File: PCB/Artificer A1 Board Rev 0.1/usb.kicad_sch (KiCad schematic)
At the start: 24 parts, among them U11 CH217K, U3 CH334F_C5187527, U5 CH217K, U6 GT-USB-7010ASV, X1 SMD-3225_4P12M12PF10PPM

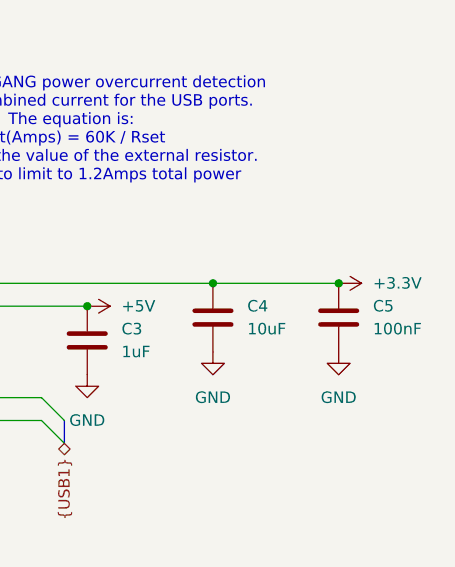
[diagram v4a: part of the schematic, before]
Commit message: added: sd, wifi, audio, started power, fixed buses
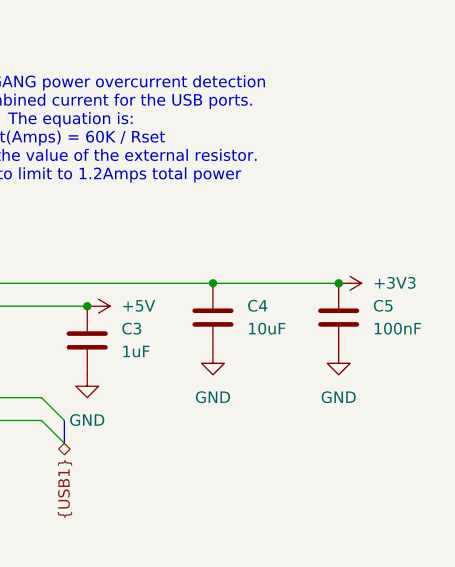
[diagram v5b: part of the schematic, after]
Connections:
- net +3.3V renamed +3V3
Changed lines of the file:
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@@
 		(company "Matthew Spotten")
 	)
-	(bus_alias "HS"
-		(members "RGMII0-PHYRSTB" "RGMII0-MDC" "RGMII0-MDIO" "RGMII0-TXD3" "RGMII0-TXD2"
-			"GMII0-TXD1" "RGMII0-TXD0" "RGMII0-TXCTL" "RGMII0-TXCK" "RGMII0-INTB"
-			"RGMII0-RXCK" "RGMII0-RXCTL" "RGMII0-RXD0" "RGMII0-RXD1" "RGMII0-RXD2"
-			"RGMII0-RXD3"
-		)
-	)
 	(text "PSELF is pulled high internally to\ntell the hub controller that it is\nself powered.\n"
 		(exclude_from_sim no)
@@
 	)
 	(junction
+		(at 267.97 66.04)
+		(diameter 0)
+		(color 0 0 0 0)
+	)
+	(junction
 		(at 121.92 73.66)
 		(diameter 0)
@@
 	)
 	(junction
-		(at 267.97 66.04)
-		(diameter 0)
-		(color 0 0 0 0)
-	)
-	(junction
 		(at 33.02 58.42)
 		(diameter 0)
@@
 	)
 	(symbol
-		(lib_id "power:+3.3V")
-		(at 267.97 66.04 270)
-		(unit 1)
-		(exclude_from_sim no)
-		(in_bom yes)
-		(on_board yes)
-		(dnp no)
-		(fields_autoplaced yes)
-		(property "Reference" "#PWR013"
-			(at 264.16 66.04 0)
-			(effects
-				(font
-					(size 1.27 1.27)
-				)
-				(hide yes)
-			)
-		)
-		(property "Value" "+3.3V"
-			(at 271.78 66.0399 90)
-			(effects
-				(font
-					(size 1.27 1.27)
-				)
-				(justify left)
-			)
-		)
-		(property "Footprint" ""
-			(at 267.97 66.04 0)
-			(effects
-				(font
-					(size 1.27 1.27)
-				)
-				(hide yes)
-			)
-		)
-		(property "Datasheet" ""
-			(at 267.97 66.04 0)
-			(effects
-				(font
-					(size 1.27 1.27)
-				)
-				(hide yes)
-			)
-		)
-		(property "Description" "Power symbol creates a global label with name \"+3.3V\""
-			(at 267.97 66.04 0)
-			(effects
-				(font
-					(size 1.27 1.27)
-				)
-				(hide yes)
-			)
-		)
-		(pin "1"
-		)
-		(instances
-			(project ""
-				(path "/7c37bdb5-94b0-4567-b5ec-a879db855389/e53cf37e-0283-4ef8-bdbb-96b13c13260b"
-					(reference "#PWR013")
-					(unit 1)
-				)
-			)
-		)
-	)
-	(symbol
 		(lib_id "Device:C")
 		(at 137.16 41.91 0)
@@
 					(unit 1)
 				)
+			)
+		)
+	)
+	(symbol
+		(lib_id "power:+3V3")
+		(at 267.97 66.04 270)
+		(unit 1)
+		(exclude_from_sim no)
+		(in_bom yes)
+		(on_board yes)
+		(dnp no)
+		(fields_autoplaced yes)
+		(property "Reference" "#PWR0201"
+			(at 264.16 66.04 0)
+			(effects
+				(font
+					(size 1.27 1.27)
+				)
+				(hide yes)
+			)
+		)
+		(property "Value" "+3V3"
+			(at 271.78 66.0399 90)
+			(effects
+				(font
+					(size 1.27 1.27)
+				)
+				(justify left)
+			)
+		)
+		(property "Footprint" ""
+			(at 267.97 66.04 0)
+			(effects
+				(font
+					(size 1.27 1.27)
+				)
+				(hide yes)
+			)
+		)
+		(property "Datasheet" ""
+			(at 267.97 66.04 0)
+			(effects
+				(font
+					(size 1.27 1.27)
+				)
+				(hide yes)
+			)
+		)
+		(property "Description" "Power symbol creates a global label with name \"+3V3\""
+			(at 267.97 66.04 0)
+			(effects
+				(font
+					(size 1.27 1.27)
+				)
+				(hide yes)
+			)
+		)
+		(pin "1"
+		)
+		(instances
+			(project "Artificer A1 Board Rev 0.1"
+				(path "/7c37bdb5-94b0-4567-b5ec-a879db855389/e53cf37e-0283-4ef8-bdbb-96b13c13260b"
+					(reference "#PWR0201")
+					(unit 1)
+				)

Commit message: added features
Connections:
- net +5V renamed 5V_SYS
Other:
- note added: "0.5Amps"
- note added: "I would like this to be two directinonal so that board could be powered from the USB C. I would need to do some work to get that working in both direction so that it can be powered and give power from this port"
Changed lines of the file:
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@@
 		(company "Matthew Spotten")
+	)
+	(bus_alias "USB1"
+		(members "USB1-DP" "USB1-DM")
+	)
+	(bus_alias "USB_DRD"
+		(members "DP" "DM" "UART0_TX" "UART0_RX")
 	)
 	(text "PSELF is pulled high internally to\ntell the hub controller that it is\nself powered.\n"
@@
 		)
 	)
+	(text "0.5Amps"
+		(exclude_from_sim no)
+		(at 210.82 111.252 0)
+		(effects
+			(font
+				(size 1.27 1.27)
+			)
+		)
+	)
 	(text "12MHz crystal. 12pF load capacitance.\n\nAssuming 5pF pin capacitance, 5pF pcb board\nmaybe two 4pF capacitors.\nI am still going to consiter this later and\nlearn more about setting up crystals\n"
 		(exclude_from_sim no)
@@
 		(exclude_from_sim no)
 		(at 238.76 29.972 0)
+		(effects
+			(font
+				(size 1.27 1.27)
+			)
+		)
+	)
+	(text "I would like this to be two directinonal so that board could\nbe powered from the USB C.\nI would need to do some work to get that working in both\ndirection so that it can be powered and give power from\nthis port"
+		(exclude_from_sim no)
+		(at 192.786 105.41 0)
 		(effects
 			(font
@@
 			)
 		)
-		(property "Value" "+5V"
+		(property "Value" "5V_SYS"
 			(at 243.84 68.5799 90)
 			(effects
@@
 		(on_board yes)
 		(dnp no)
-		(fields_autoplaced yes)
 		(property "Reference" "#PWR051"
 			(at 264.16 114.3 0)
@@
 			)
 		)
-		(property "Value" "+5V"
-			(at 264.16 105.41 0)
-			(effects
-				(font
-					(size 1.27 1.27)
-				)
+		(property "Value" "5V_SYS"
+			(at 261.112 106.172 0)
+			(effects
+				(font
+					(size 1.27 1.27)
+				)
+				(justify left)
 			)
 		)
@@
 		(on_board yes)
 		(dnp no)
-		(fields_autoplaced yes)
 		(property "Reference" "#PWR011"
 			(at 190.5 27.94 0)
@@
 			)
 		)
-		(property "Value" "+5V"
-			(at 190.5 19.05 0)
-			(effects
-				(font
-					(size 1.27 1.27)
-				)
-			)
-		)
+		(property "Value" "5V_SYS"
+			(at 186.944 19.812 0)
+			(effects
+				(font
+					(size 1.27 1.27)
+				)
+				(justify left)
+			)
+		)

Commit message: finished rough draft of power supply circuitry!
Yay! This one took a while
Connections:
- net +3V3 renamed VCC-3V3
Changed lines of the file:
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@@
 	)
 	(junction
-		(at 267.97 66.04)
-		(diameter 0)
-		(color 0 0 0 0)
-	)
-	(junction
 		(at 121.92 73.66)
 		(diameter 0)
@@
 		(color 0 0 0 0)
 	)
+	(junction
+		(at 267.97 66.04)
+		(diameter 0)
+		(color 0 0 0 0)
+	)
 	(no_connect
 		(at 194.31 63.5)
@@
 	(wire
 		(pts
+			(xy 267.97 62.23) (xy 267.97 66.04)
+		)
+		(stroke
+			(width 0)
+			(type default)
+		)
+	)
+	(wire
+		(pts
 			(xy 135.89 87.63) (xy 121.92 87.63)
 		)
@@
 	)
 	(symbol
+		(lib_id "power:+5V")
+		(at 267.97 62.23 0)
+		(unit 1)
+		(exclude_from_sim no)
+		(in_bom yes)
+		(on_board yes)
+		(dnp no)
+		(property "Reference" "#PWR0395"
+			(at 267.97 66.04 0)
+			(effects
+				(font
+					(size 1.27 1.27)
+				)
+				(hide yes)
+			)
+		)
+		(property "Value" "VCC-3V3"
+			(at 260.096 60.706 0)
+			(effects
+				(font
+					(size 1.27 1.27)
+				)
+			)
+		)
+		(property "Footprint" ""
+			(at 267.97 62.23 0)
+			(effects
+				(font
+					(size 1.27 1.27)
+				)
+				(hide yes)
+			)
+		)
+		(property "Datasheet" ""
+			(at 267.97 62.23 0)
+			(effects
+				(font
+					(size 1.27 1.27)
+				)
+				(hide yes)
+			)
+		)
+		(property "Description" "Power symbol creates a global label with name \"+5V\""
+			(at 267.97 62.23 0)
+			(effects
+				(font
+					(size 1.27 1.27)
+				)
+				(hide yes)
+			)
+		)
+		(pin "1"
+		)
+		(instances
+			(project "Artificer A1 Board Rev 0.1"
+				(path "/7c37bdb5-94b0-4567-b5ec-a879db855389/e53cf37e-0283-4ef8-bdbb-96b13c13260b"
+					(reference "#PWR0395")
+					(unit 1)
+				)
+			)
+		)
+	)
+	(symbol
 		(lib_id "Device:C")
 		(at 264.16 116.84 180)
@@
 					(unit 1)
 				)
-			)
-		)
-	)
-	(symbol
-		(lib_id "power:+3V3")
-		(at 267.97 66.04 270)
-		(unit 1)
-		(exclude_from_sim no)
-		(in_bom yes)
-		(on_board yes)
-		(dnp no)
-		(fields_autoplaced yes)
-		(property "Reference" "#PWR0201"
-			(at 264.16 66.04 0)
-			(effects
-				(font
-					(size 1.27 1.27)
-				)
-				(hide yes)
-			)
-		)
-		(property "Value" "+3V3"
-			(at 271.78 66.0399 90)
-			(effects
-				(font
-					(size 1.27 1.27)
-				)
-				(justify left)
-			)
-		)
-		(property "Footprint" ""
-			(at 267.97 66.04 0)
-			(effects
-				(font
-					(size 1.27 1.27)
-				)
-				(hide yes)
-			)
-		)
-		(property "Datasheet" ""
-			(at 267.97 66.04 0)
-			(effects
-				(font
-					(size 1.27 1.27)
-				)
-				(hide yes)
-			)
-		)
-		(property "Description" "Power symbol creates a global label with name \"+3V3\""
-			(at 267.97 66.04 0)
-			(effects
-				(font
-					(size 1.27 1.27)
-				)
-				(hide yes)
-			)
-		)
-		(pin "1"
-		)
-		(instances
-			(project "Artificer A1 Board Rev 0.1"
-				(path "/7c37bdb5-94b0-4567-b5ec-a879db855389/e53cf37e-0283-4ef8-bdbb-96b13c13260b"
-					(reference "#PWR0201")
-					(unit 1)
-				)
